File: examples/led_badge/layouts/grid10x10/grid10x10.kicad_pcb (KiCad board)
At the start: 4 copper layers, 200 parts

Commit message: rebuild lad badge
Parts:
- C1, C10, C100, C11, C12, C13, C14, C15, C16, C17, C18, C19, C2, C20, C21, C22, C23, C24, C25, C26, C27, C28, C29, C3, C30, C31, C32, C33, C34, C35, C36, C37, C38, C39, C4, C40, C41, C42, C43, C44, C45, C46, C47, C48, C49, C5, C50, C51, C52, C53, C54, C55, C56, C57, C58, C59, C6, C60, C61, C62, C63, C64, C65, C66, C67, C68, C69, C7, C70, C71, C72, C73, C74, C75, C76, C77, C78, C79, C8, C80, C81, C82, C83, C84, C85, C86, C87, C88, C89, C9, C90, C91, C92, C93, C94, C95, C96, C97, C98, C99: value 100nF ±10% 16V X7R -> 100nF ±10% 50V X7R; footprint Samsung_Electro_Mechanics_CL05B104KO5NNNC:C0402 -> Samsung_Electro_Mechanics_CL05B104KB54PNC:C0402
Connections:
- net -line-0 renamed rows[0]-data_in-line
- net -line-1 renamed data_out-line
- net -line-10 renamed rows[9]-data_in-line
- net -line-2 renamed rows[1]-data_in-line
- net -line-3 renamed rows[2]-data_in-line
- net -line-4 renamed rows[3]-data_in-line
- net -line-5 renamed rows[4]-data_in-line
- net -line-6 renamed rows[5]-data_in-line
- net -line-7 renamed rows[6]-data_in-line
- net -line-8 renamed rows[7]-data_in-line
- net -line-9 renamed rows[8]-data_in-line
- net gnd renamed GND
- net hv renamed VCC
- net rows[0]-DOUT-0 renamed leds[1]-data_in-DIN-0
- net rows[0]-DOUT-1 renamed leds[2]-data_in-DIN-0
- net rows[0]-DOUT-2 renamed leds[3]-data_in-DIN-0
- net rows[0]-DOUT-3 renamed leds[4]-data_in-DIN-0
- net rows[0]-DOUT-4 renamed leds[5]-data_in-DIN-0
- net rows[0]-DOUT-5 renamed leds[6]-data_in-DIN-0
- net rows[0]-DOUT-6 renamed leds[7]-data_in-DIN-0
- net rows[0]-DOUT-7 renamed leds[8]-data_in-DIN-0
- net rows[0]-DOUT-8 renamed leds[9]-data_in-DIN-0
- net rows[1]-DOUT-0 renamed leds[1]-data_in-DIN-1
- net rows[1]-DOUT-1 renamed leds[2]-data_in-DIN-1
- net rows[1]-DOUT-2 renamed leds[3]-data_in-DIN-1
- net rows[1]-DOUT-3 renamed leds[4]-data_in-DIN-1
- net rows[1]-DOUT-4 renamed leds[5]-data_in-DIN-1
- net rows[1]-DOUT-5 renamed leds[6]-data_in-DIN-1
- net rows[1]-DOUT-6 renamed leds[7]-data_in-DIN-1
- net rows[1]-DOUT-7 renamed leds[8]-data_in-DIN-1
- net rows[1]-DOUT-8 renamed leds[9]-data_in-DIN-1
- net rows[2]-DOUT-0 renamed leds[1]-data_in-DIN-2
- net rows[2]-DOUT-1 renamed leds[2]-data_in-DIN-2
- net rows[2]-DOUT-2 renamed leds[3]-data_in-DIN-2
- net rows[2]-DOUT-3 renamed leds[4]-data_in-DIN-2
- net rows[2]-DOUT-4 renamed leds[5]-data_in-DIN-2
- net rows[2]-DOUT-5 renamed leds[6]-data_in-DIN-2
- net rows[2]-DOUT-6 renamed leds[7]-data_in-DIN-2
- net rows[2]-DOUT-7 renamed leds[8]-data_in-DIN-2
- net rows[2]-DOUT-8 renamed leds[9]-data_in-DIN-2
- net rows[3]-DOUT-0 renamed leds[1]-data_in-DIN-3
- net rows[3]-DOUT-1 renamed leds[2]-data_in-DIN-3
- net rows[3]-DOUT-2 renamed leds[3]-data_in-DIN-3
- net rows[3]-DOUT-3 renamed leds[4]-data_in-DIN-3
- net rows[3]-DOUT-4 renamed leds[5]-data_in-DIN-3
- net rows[3]-DOUT-5 renamed leds[6]-data_in-DIN-3
- net rows[3]-DOUT-6 renamed leds[7]-data_in-DIN-3
- net rows[3]-DOUT-7 renamed leds[8]-data_in-DIN-3
- net rows[3]-DOUT-8 renamed leds[9]-data_in-DIN-3
- net rows[4]-DOUT-0 renamed leds[1]-data_in-DIN-4
- net rows[4]-DOUT-1 renamed leds[2]-data_in-DIN-4
- net rows[4]-DOUT-2 renamed leds[3]-data_in-DIN-4
- net rows[4]-DOUT-3 renamed leds[4]-data_in-DIN-4
- net rows[4]-DOUT-4 renamed leds[5]-data_in-DIN-4
- net rows[4]-DOUT-5 renamed leds[6]-data_in-DIN-4
- net rows[4]-DOUT-6 renamed leds[7]-data_in-DIN-4
- net rows[4]-DOUT-7 renamed leds[8]-data_in-DIN-4
- net rows[4]-DOUT-8 renamed leds[9]-data_in-DIN-4
- net rows[5]-DOUT-0 renamed leds[1]-data_in-DIN-5
- net rows[5]-DOUT-1 renamed leds[2]-data_in-DIN-5
- net rows[5]-DOUT-2 renamed leds[3]-data_in-DIN-5
- net rows[5]-DOUT-3 renamed leds[4]-data_in-DIN-5
- net rows[5]-DOUT-4 renamed leds[5]-data_in-DIN-5
- net rows[5]-DOUT-5 renamed leds[6]-data_in-DIN-5
- net rows[5]-DOUT-6 renamed leds[7]-data_in-DIN-5
- net rows[5]-DOUT-7 renamed leds[8]-data_in-DIN-5
- net rows[5]-DOUT-8 renamed leds[9]-data_in-DIN-5
- net rows[6]-DOUT-0 renamed leds[1]-data_in-DIN-6
- net rows[6]-DOUT-1 renamed leds[2]-data_in-DIN-6
- net rows[6]-DOUT-2 renamed leds[3]-data_in-DIN-6
- net rows[6]-DOUT-3 renamed leds[4]-data_in-DIN-6
- net rows[6]-DOUT-4 renamed leds[5]-data_in-DIN-6
- net rows[6]-DOUT-5 renamed leds[6]-data_in-DIN-6
- net rows[6]-DOUT-6 renamed leds[7]-data_in-DIN-6
- net rows[6]-DOUT-7 renamed leds[8]-data_in-DIN-6
- net rows[6]-DOUT-8 renamed leds[9]-data_in-DIN-6
- net rows[7]-DOUT-0 renamed leds[1]-data_in-DIN-7
- net rows[7]-DOUT-1 renamed leds[2]-data_in-DIN-7
- net rows[7]-DOUT-2 renamed leds[3]-data_in-DIN-7
- net rows[7]-DOUT-3 renamed leds[4]-data_in-DIN-7
- net rows[7]-DOUT-4 renamed leds[5]-data_in-DIN-7
- net rows[7]-DOUT-5 renamed leds[6]-data_in-DIN-7
- net rows[7]-DOUT-6 renamed leds[7]-data_in-DIN-7
- net rows[7]-DOUT-7 renamed leds[8]-data_in-DIN-7
- net rows[7]-DOUT-8 renamed leds[9]-data_in-DIN-7
- net rows[8]-DOUT-0 renamed leds[1]-data_in-DIN-8
- net rows[8]-DOUT-1 renamed leds[2]-data_in-DIN-8
- net rows[8]-DOUT-2 renamed leds[3]-data_in-DIN-8
- net rows[8]-DOUT-3 renamed leds[4]-data_in-DIN-8
- net rows[8]-DOUT-4 renamed leds[5]-data_in-DIN-8
- net rows[8]-DOUT-5 renamed leds[6]-data_in-DIN-8
- net rows[8]-DOUT-6 renamed leds[7]-data_in-DIN-8
- net rows[8]-DOUT-7 renamed leds[8]-data_in-DIN-8
- net rows[8]-DOUT-8 renamed leds[9]-data_in-DIN-8
- net rows[9]-DOUT-0 renamed leds[1]-data_in-DIN-9
- net rows[9]-DOUT-1 renamed leds[2]-data_in-DIN-9
- net rows[9]-DOUT-2 renamed leds[3]-data_in-DIN-9
- net rows[9]-DOUT-3 renamed leds[4]-data_in-DIN-9
- net rows[9]-DOUT-4 renamed leds[5]-data_in-DIN-9
- net rows[9]-DOUT-5 renamed leds[6]-data_in-DIN-9
- net rows[9]-DOUT-6 renamed leds[7]-data_in-DIN-9
- net rows[9]-DOUT-7 renamed leds[8]-data_in-DIN-9
- net rows[9]-DOUT-8 renamed leds[9]-data_in-DIN-9

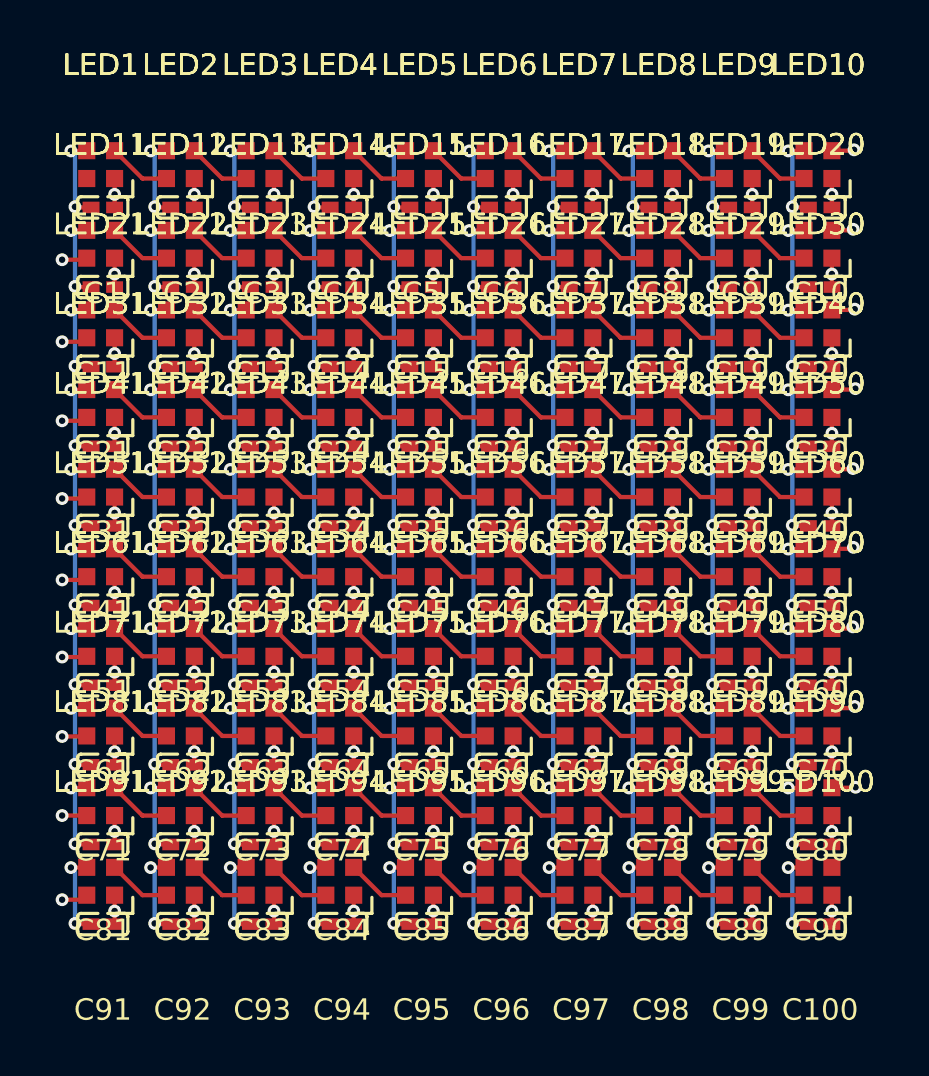
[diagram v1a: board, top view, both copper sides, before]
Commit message: fix import and layout led badge (badge target still fails)
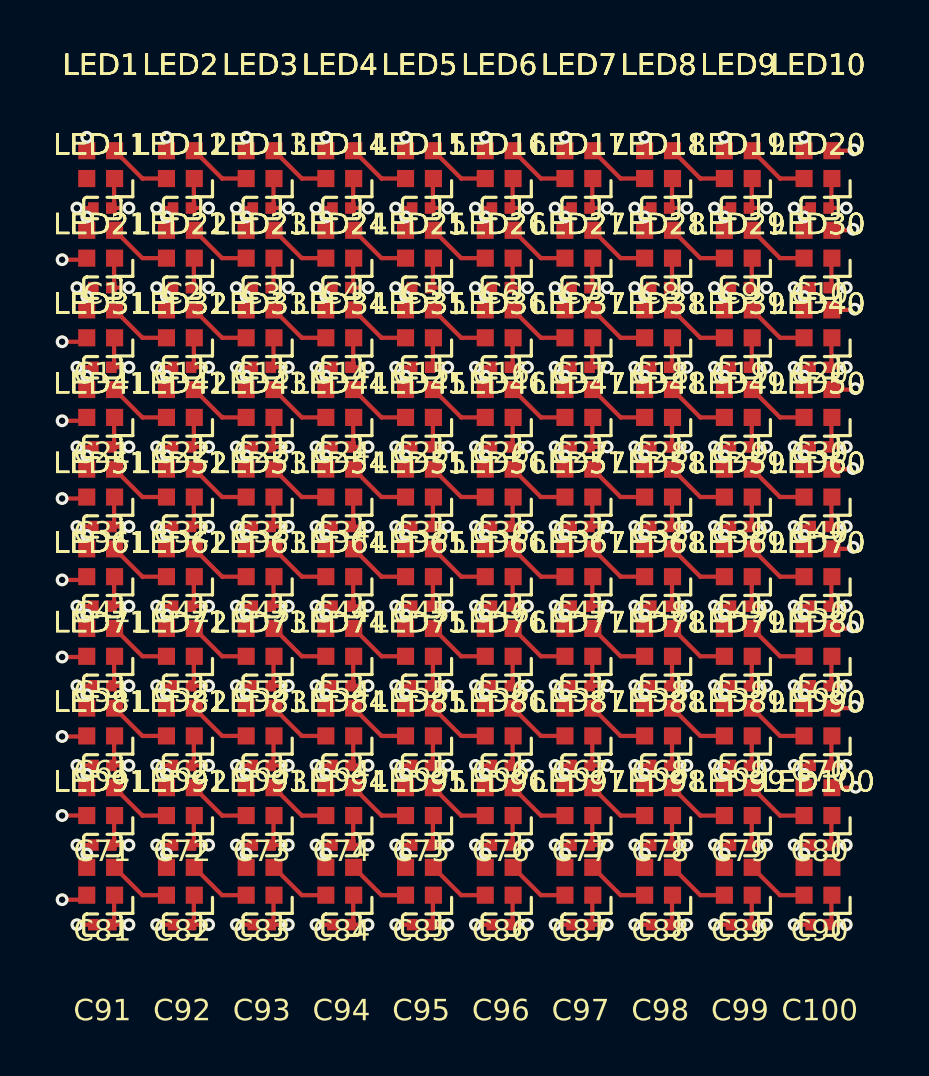
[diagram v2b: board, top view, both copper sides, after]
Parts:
- C1, C10, C100, C11, C12, C13, C14, C15, C16, C17, C18, C19, C2, C20, C21, C22, C23, C24, C25, C26, C27, C28, C29, C3, C30, C31, C32, C33, C34, C35, C36, C37, C38, C39, C4, C40, C41, C42, C43, C44, C45, C46, C47, C48, C49, C5, C50, C51, C52, C53, C54, C55, C56, C57, C58, C59, C6, C60, C61, C62, C63, C64, C65, C66, C67, C68, C69, C7, C70, C71, C72, C73, C74, C75, C76, C77, C78, C79, C8, C80, C81, C82, C83, C84, C85, C86, C87, C88, C89, C9, C90, C91, C92, C93, C94, C95, C96, C97, C98, C99: value 100nF ±10% 50V X7R -> 0F; footprint Samsung_Electro_Mechanics_CL05B104KB54PNC:C0402 -> Samsung_Electro_Mechanics_CL05B104KO5NNNC:C0402
- LED1, LED10, LED100, LED11, LED12, LED13, LED14, LED15, LED16, LED17, LED18, LED19, LED2, LED20, LED21, LED22, LED23, LED24, LED25, LED26, LED27, LED28, LED29, LED3, LED30, LED31, LED32, LED33, LED34, LED35, LED36, LED37, LED38, LED39, LED4, LED40, LED41, LED42, LED43, LED44, LED45, LED46, LED47, LED48, LED49, LED5, LED50, LED51, LED52, LED53, LED54, LED55, LED56, LED57, LED58, LED59, LED6, LED60, LED61, LED62, LED63, LED64, LED65, LED66, LED67, LED68, LED69, LED7, LED70, LED71, LED72, LED73, LED74, LED75, LED76, LED77, LED78, LED79, LED8, LED80, LED81, LED82, LED83, LED84, LED85, LED86, LED87, LED88, LED89, LED9, LED90, LED91, LED92, LED93, LED94, LED95, LED96, LED97, LED98, LED99: footprint OPSCO_SK6805_EC20:LED-SMD_4P-L2.0-W2.0-BR -> OPSCO_Optoelectronics_SK6805_EC20:LED-SMD_4P-L2.0-W2.0-BR
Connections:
- net GND renamed lv
- net VCC renamed hv
- net leds[1]-data_in-DIN-0 renamed DIN
- net leds[2]-data_in-DIN-0 renamed leds[2]-data_in-DIN
- net leds[3]-data_in-DIN-0 renamed leds[3]-data_in-DIN
- net leds[4]-data_in-DIN-0 renamed leds[4]-data_in-DIN
- net leds[5]-data_in-DIN-0 renamed leds[5]-data_in-DIN
- net leds[6]-data_in-DIN-0 renamed leds[6]-data_in-DIN
- net leds[7]-data_in-DIN-0 renamed leds[7]-data_in-DIN
- net leds[8]-data_in-DIN-0 renamed leds[8]-data_in-DIN
- net leds[9]-data_in-DIN-0 renamed leds[9]-data_in-DIN
- net rows[0]-data_in-line renamed line
- LED11 pad 2: leds[1]-data_in-DIN-1 -> leds[1]-data_in-DIN
- LED12 pad 4: leds[1]-data_in-DIN-1 -> leds[1]-data_in-DIN
- LED21 pad 2: leds[1]-data_in-DIN-2 -> leds[1]-data_in-DIN-1
- LED22 pad 4: leds[1]-data_in-DIN-2 -> leds[1]-data_in-DIN-1
- LED31 pad 2: leds[1]-data_in-DIN-3 -> leds[1]-data_in-DIN-2
- LED32 pad 4: leds[1]-data_in-DIN-3 -> leds[1]-data_in-DIN-2
- LED41 pad 2: leds[1]-data_in-DIN-4 -> leds[1]-data_in-DIN-3
- LED42 pad 4: leds[1]-data_in-DIN-4 -> leds[1]-data_in-DIN-3
- LED51 pad 2: leds[1]-data_in-DIN-5 -> leds[1]-data_in-DIN-4
- LED52 pad 4: leds[1]-data_in-DIN-5 -> leds[1]-data_in-DIN-4
- LED61 pad 2: leds[1]-data_in-DIN-6 -> leds[1]-data_in-DIN-5
- LED62 pad 4: leds[1]-data_in-DIN-6 -> leds[1]-data_in-DIN-5
- LED71 pad 2: leds[1]-data_in-DIN-7 -> leds[1]-data_in-DIN-6
- LED72 pad 4: leds[1]-data_in-DIN-7 -> leds[1]-data_in-DIN-6
- LED81 pad 2: leds[1]-data_in-DIN-8 -> leds[1]-data_in-DIN-7
- LED82 pad 4: leds[1]-data_in-DIN-8 -> leds[1]-data_in-DIN-7
- LED91 pad 2: leds[1]-data_in-DIN-9 -> leds[1]-data_in-DIN-8
- LED92 pad 4: leds[1]-data_in-DIN-9 -> leds[1]-data_in-DIN-8
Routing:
- net lv: track 419.5 -> 165.2 mm
- net hv: track 173.8 -> 207.8 mm
- net leds[1]-data_in-DIN: track 0.00 -> 2.96 mm
- net leds[1]-data_in-DIN-9: track 2.96 -> 0.00 mm

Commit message: fix led badge strip/grid builds
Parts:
- C1, C10, C100, C11, C12, C13, C14, C15, C16, C17, C18, C19, C2, C20, C21, C22, C23, C24, C25, C26, C27, C28, C29, C3, C30, C31, C32, C33, C34, C35, C36, C37, C38, C39, C4, C40, C41, C42, C43, C44, C45, C46, C47, C48, C49, C5, C50, C51, C52, C53, C54, C55, C56, C57, C58, C59, C6, C60, C61, C62, C63, C64, C65, C66, C67, C68, C69, C7, C70, C71, C72, C73, C74, C75, C76, C77, C78, C79, C8, C80, C81, C82, C83, C84, C85, C86, C87, C88, C89, C9, C90, C91, C92, C93, C94, C95, C96, C97, C98, C99: value 0F -> 100nF
